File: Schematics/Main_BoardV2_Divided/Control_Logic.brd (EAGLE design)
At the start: 151.1 x 125.4 mm, 77 parts

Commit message: Visual Improvments
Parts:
- SV17: device con-lstb:MA08-1 -> pinhead:1X08
- SV23: device con-lstb:MA08-2 -> pinhead:2X08
- flipped JP12 to the top, turned to 180 degrees
- flipped JP13 to the top, turned to 180 degrees
- flipped JP5 to the top, turned to 180 degrees
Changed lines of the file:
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@@
 </layers>
 <board>
-<fusionsync huburn="a.cGVyc29uYWw6dWUyYzAxZDJj" projecturn="a.cGVyc29uYWw6dWUyYzAxZDJjIzIwMTkwNTA1MTkyMDg5NTI2" f3durn="urn:adsk.wipprod:dm.lineage:5vW4CCZ3SoaiVhg5slD4Gg" pcbguid="fc1e82cf-980c-4085-b012-4696e4d23687" lastpulledtime="" lastsyncedchangeguid="9388281c-1932-1015-b2ac-b4e115ec7e99"/>
+<fusionsync huburn="a.cGVyc29uYWw6dWUyYzAxZDJj" projecturn="a.cGVyc29uYWw6dWUyYzAxZDJjIzIwMTkwNTA1MTkyMDg5NTI2" f3durn="urn:adsk.wipprod:dm.lineage:5vW4CCZ3SoaiVhg5slD4Gg" pcbguid="fc1e82cf-980c-4085-b012-4696e4d23687" lastpulledtime="" lastsyncedchangeguid="d297562d-cfa8-3444-ce06-3ef9c99cdce7"/>
 <plain>
 <wire x1="0" y1="1.27" x2="151.11" y2="1.27" width="0" layer="20"/>
@@
 <attribute name="VALUE" x="44.45" y="105.41" size="0.9906" layer="27" ratio="10" rot="R90"/>
 </element>
-<element name="SV17" library="con-lstb" library_urn="urn:adsk.eagle:library:162" package="MA08-1" package3d_urn="urn:adsk.eagle:package:8343/1" value="" x="6.35" y="99.06" smashed="yes" rot="R90">
+<element name="SV17" library="pinhead" library_urn="urn:adsk.eagle:library:325" package="1X08" package3d_urn="urn:adsk.eagle:package:22409/2" value="" x="6.35" y="99.06" smashed="yes" rot="R90">
 <attribute name="MF" value="" x="6.35" y="99.06" size="1.778" layer="27" rot="R90" display="off"/>
 <attribute name="MPN" value="" x="6.35" y="99.06" size="1.778" layer="27" rot="R90" display="off"/>
@@
 <attribute name="VALUE" x="6.35" y="99.06" size="1.27" layer="27" ratio="10" rot="R90"/>
 </element>
-<element name="JP5" library="pinhead" library_urn="urn:adsk.eagle:library:325" package="1X02" package3d_urn="urn:adsk.eagle:package:22435/2" value="" x="113.03" y="115.57" smashed="yes" rot="MR0">
-<attribute name="NAME" x="115.6462" y="117.3988" size="1.27" layer="26" ratio="10" rot="MR0"/>
-<attribute name="VALUE" x="115.57" y="112.395" size="1.27" layer="28" rot="MR0"/>
+<element name="JP5" library="pinhead" library_urn="urn:adsk.eagle:library:325" package="1X02" package3d_urn="urn:adsk.eagle:package:22435/2" value="" x="113.03" y="115.57" smashed="yes" rot="R180">
+<attribute name="NAME" x="115.6462" y="113.7412" size="1.27" layer="25" ratio="10" rot="R180"/>
+<attribute name="VALUE" x="115.57" y="118.745" size="1.27" layer="27" rot="R180"/>
 </element>
 <element name="JP10" library="pinhead" library_urn="urn:adsk.eagle:library:325" package="1X02" package3d_urn="urn:adsk.eagle:package:22435/2" value="" x="6.35" y="71.12" smashed="yes" rot="R90">
@@
 <attribute name="VALUE" x="3.175" y="58.42" size="1.27" layer="27" rot="R270"/>
 </element>
-<element name="JP12" library="pinhead" library_urn="urn:adsk.eagle:library:325" package="1X02" package3d_urn="urn:adsk.eagle:package:22435/2" value="" x="120.65" y="115.57" smashed="yes" rot="MR0">
-<attribute name="NAME" x="123.2662" y="117.3988" size="1.27" layer="26" ratio="10" rot="MR0"/>
-<attribute name="VALUE" x="123.19" y="112.395" size="1.27" layer="28" rot="MR0"/>
-</element>
-<element name="JP13" library="pinhead" library_urn="urn:adsk.eagle:library:325" package="1X02" package3d_urn="urn:adsk.eagle:package:22435/2" value="" x="105.41" y="115.57" smashed="yes" rot="MR0">
-<attribute name="NAME" x="108.0262" y="117.3988" size="1.27" layer="26" ratio="10" rot="MR0"/>
-<attribute name="VALUE" x="107.95" y="112.395" size="1.27" layer="28" rot="MR0"/>
+<element name="JP12" library="pinhead" library_urn="urn:adsk.eagle:library:325" package="1X02" package3d_urn="urn:adsk.eagle:package:22435/2" value="" x="120.65" y="115.57" smashed="yes" rot="R180">
+<attribute name="NAME" x="123.2662" y="113.7412" size="1.27" layer="25" ratio="10" rot="R180"/>
+<attribute name="VALUE" x="123.19" y="118.745" size="1.27" layer="27" rot="R180"/>
+</element>
+<element name="JP13" library="pinhead" library_urn="urn:adsk.eagle:library:325" package="1X02" package3d_urn="urn:adsk.eagle:package:22435/2" value="" x="105.41" y="115.57" smashed="yes" rot="R180">
+<attribute name="NAME" x="108.0262" y="113.7412" size="1.27" layer="25" ratio="10" rot="R180"/>
+<attribute name="VALUE" x="107.95" y="118.745" size="1.27" layer="27" rot="R180"/>
 </element>
 <element name="JP14" library="pinhead" library_urn="urn:adsk.eagle:library:325" package="1X02" package3d_urn="urn:adsk.eagle:package:22435/2" value="" x="6.35" y="63.5" smashed="yes" rot="R90">
@@
 <attribute name="VALUE" x="9.525" y="60.96" size="1.27" layer="27" rot="R90"/>
 </element>
-<element name="SV23" library="con-lstb" library_urn="urn:adsk.eagle:library:162" package="MA08-2" package3d_urn="urn:adsk.eagle:package:8335/1" value="" x="142.24" y="39.37" smashed="yes" rot="R270">
+<element name="SV23" library="pinhead" library_urn="urn:adsk.eagle:library:325" package="2X08" package3d_urn="urn:adsk.eagle:package:22481/2" value="" x="142.24" y="39.37" smashed="yes" rot="R270">
 <attribute name="MF" value="" x="142.24" y="39.37" size="1.778" layer="27" rot="R270" display="off"/>
 <attribute name="MPN" value="" x="142.24" y="39.37" size="1.778" layer="27" rot="R270" display="off"/>
@@
 <wire x1="95.5548" y1="98.933" x2="111.2393" y2="114.6175" width="0.254" layer="1"/>
 <wire x1="92.9005" y1="90.2462" x2="92.9005" y2="96.2787" width="0.254" layer="1"/>
-<wire x1="111.7219" y1="115.3414" x2="111.76" y2="115.57" width="0.254" layer="1"/>
+<wire x1="111.7219" y1="115.3414" x2="111.76" y2="115.57" width="0.254" layer="16"/>
 <wire x1="92.9005" y1="90.2462" x2="92.71" y2="90.17" width="0.254" layer="1"/>
 <wire x1="125.7173" y1="71.9074" x2="125.7173" y2="71.1835" width="0.254" layer="1"/>
@@
 <wire x1="128.511984375" y1="18.427015625" x2="128.27" y2="18.427015625" width="0.254" layer="16"/>
 <wire x1="128.141284375" y1="18.869796875" x2="128.27" y2="18.427015625" width="0.254" layer="16"/>
+<wire x1="111.7219" y1="115.3414" x2="111.7219" y2="115.3414" width="0" layer="19" extent="1-16"/>
 </signal>
 <signal name="INST_REGISTER1:VCC">
@@
 <wire x1="74.5617" y1="50.9143" x2="89.7636" y2="66.1162" width="0.254" layer="1"/>
 <wire x1="73.8378" y1="50.9143" x2="74.5617" y2="50.9143" width="0.254" layer="1"/>
-<wire x1="104.0003" y1="115.3414" x2="104.14" y2="115.57" width="0.254" layer="16"/>
+<wire x1="104.0003" y1="115.3414" x2="104.14" y2="115.57" width="0.254" layer="1"/>
 <wire x1="73.8378" y1="50.9143" x2="73.66" y2="50.8" width="0.254" layer="1"/>
 <via x="89.7636" y="66.1162" extent="1-16" drill="0.35"/>
@@
 <contactref element="CONTROL_LOGIC1:IC5" pad="9"/>
 <contactref element="CONTROL_LOGIC1:IC5" pad="10"/>
+<wire x1="104.0003" y1="115.3414" x2="104.0003" y2="115.3414" width="0" layer="19" extent="1-16"/>
 </signal>
 <signal name="PC_LE">
@@
 <wire x1="32.0929" y1="110.7567" x2="55.7403" y2="110.7567" width="0.254" layer="16"/>
 <wire x1="30.1625" y1="108.8263" x2="32.0929" y2="110.7567" width="0.254" layer="16"/>
-<wire x1="106.6546" y1="115.5827" x2="106.68" y2="115.57" width="0.254" layer="16"/>
+<wire x1="106.6546" y1="115.5827" x2="106.68" y2="115.57" width="0.254" layer="1"/>
 <via x="37.6428" y="76.4921" extent="1-16" drill="0.35"/>
 <contactref element="INST_REGISTER1:IC2" pad="15"/>
 <contactref element="INST_REGISTER1:IC3" pad="15"/>
 <contactref element="CONTROL_LOGIC1:IC5" pad="8"/>
+<wire x1="106.6546" y1="115.5827" x2="106.6546" y2="115.5827" width="0" layer="19" extent="1-16"/>
 </signal>
 <signal name="|AWRITE">
@@
 <wire x1="129.8194" y1="59.1185" x2="129.8194" y2="106.4133" width="0.254" layer="1"/>
 <wire x1="128.8542" y1="58.1533" x2="129.8194" y2="59.1185" width="0.254" layer="1"/>
-<wire x1="122.0978" y1="115.3414" x2="121.92" y2="115.57" width="0.254" layer="1"/>
+<wire x1="122.0978" y1="115.3414" x2="121.92" y2="115.57" width="0.254" layer="16"/>
 <via x="128.8542" y="58.1533" extent="1-16" drill="0.35"/>
 <contactref element="CONTROL_LOGIC1:IC2" pad="8"/>
 <contactref element="CONTROL_LOGIC1:IC1" pad="8"/>
+<wire x1="122.0978" y1="115.3414" x2="122.0978" y2="115.3414" width="0" layer="19" extent="1-16"/>
 </signal>
 <signal name="CF">
@@
 <wire x1="128.8542" y1="68.0466" x2="128.8542" y2="105.6894" width="0.254" layer="1"/>
 <wire x1="128.1303" y1="67.3227" x2="128.8542" y2="68.0466" width="0.254" layer="16"/>
-<wire x1="119.4435" y1="115.3414" x2="119.38" y2="115.57" width="0.254" layer="1"/>
+<wire x1="119.4435" y1="115.3414" x2="119.38" y2="115.57" width="0.254" layer="16"/>
 <via x="127.1651" y="39.5732" extent="1-16" drill="0.35"/>
 <via x="128.8542" y="68.0466" extent="1-16" drill="0.35"/>
 <contactref element="CONTROL_LOGIC1:IC2" pad="7"/>
 <contactref element="CONTROL_LOGIC1:IC1" pad="7"/>
+<wire x1="119.4435" y1="115.3414" x2="119.4435" y2="115.3414" width="0" layer="19" extent="1-16"/>
 </signal>
 <signal name="RAM_LRS">

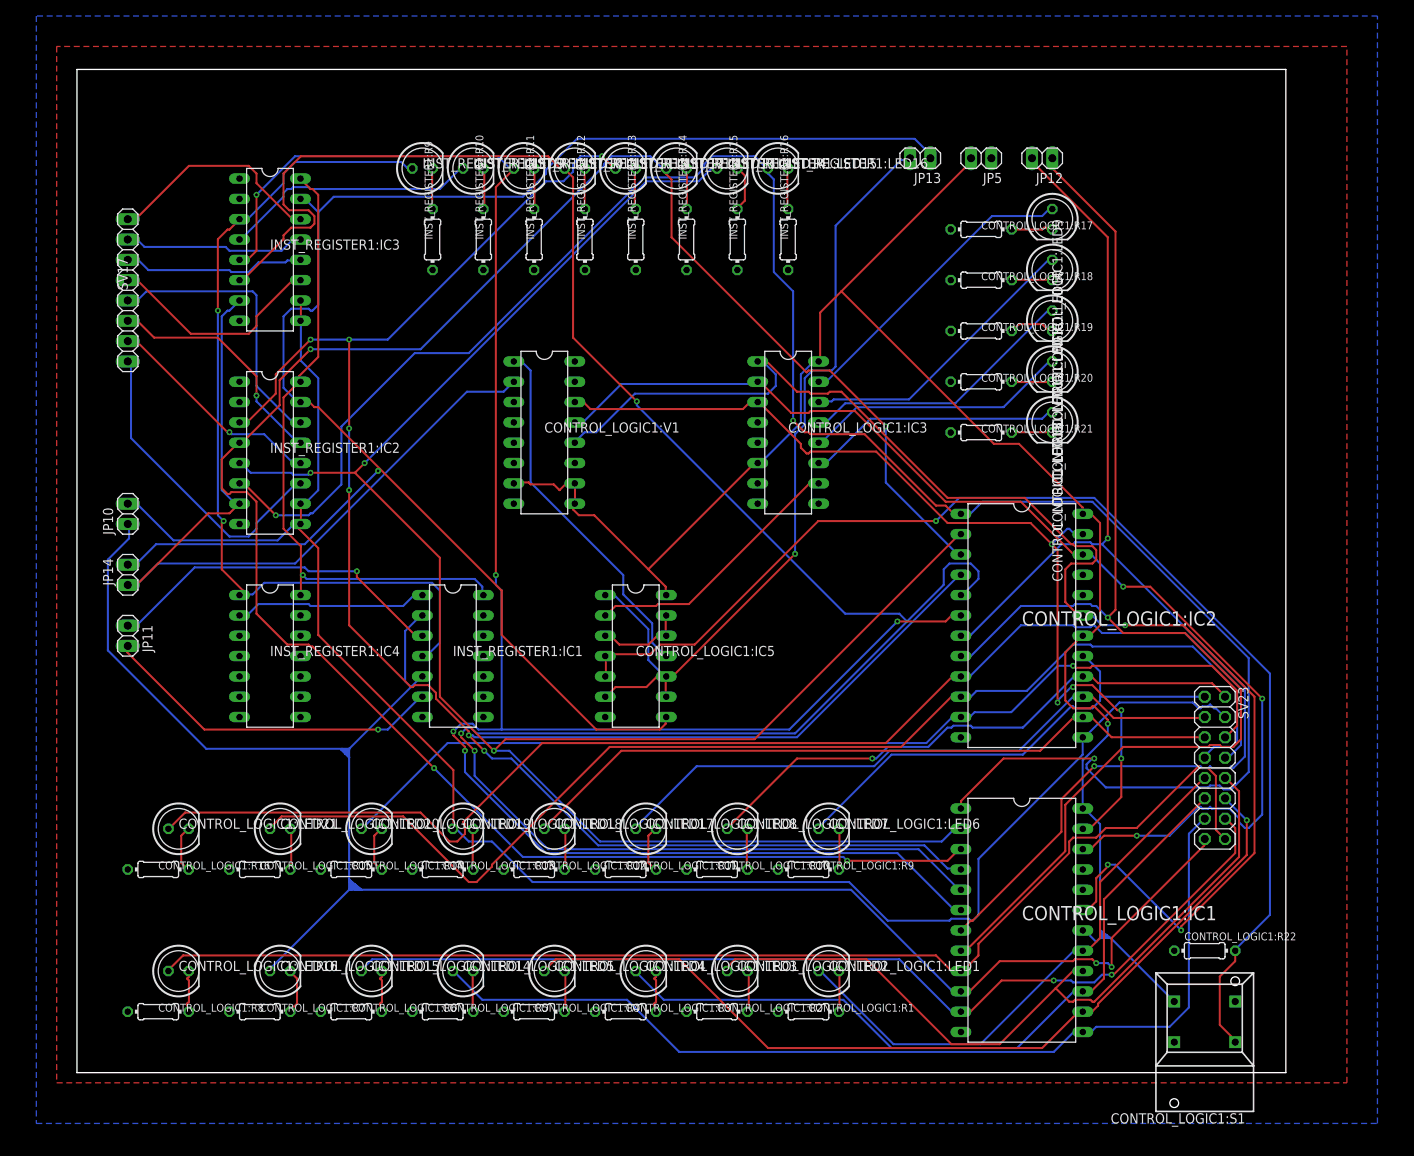
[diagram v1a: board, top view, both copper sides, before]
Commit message: Microcode Added and Ram Updated
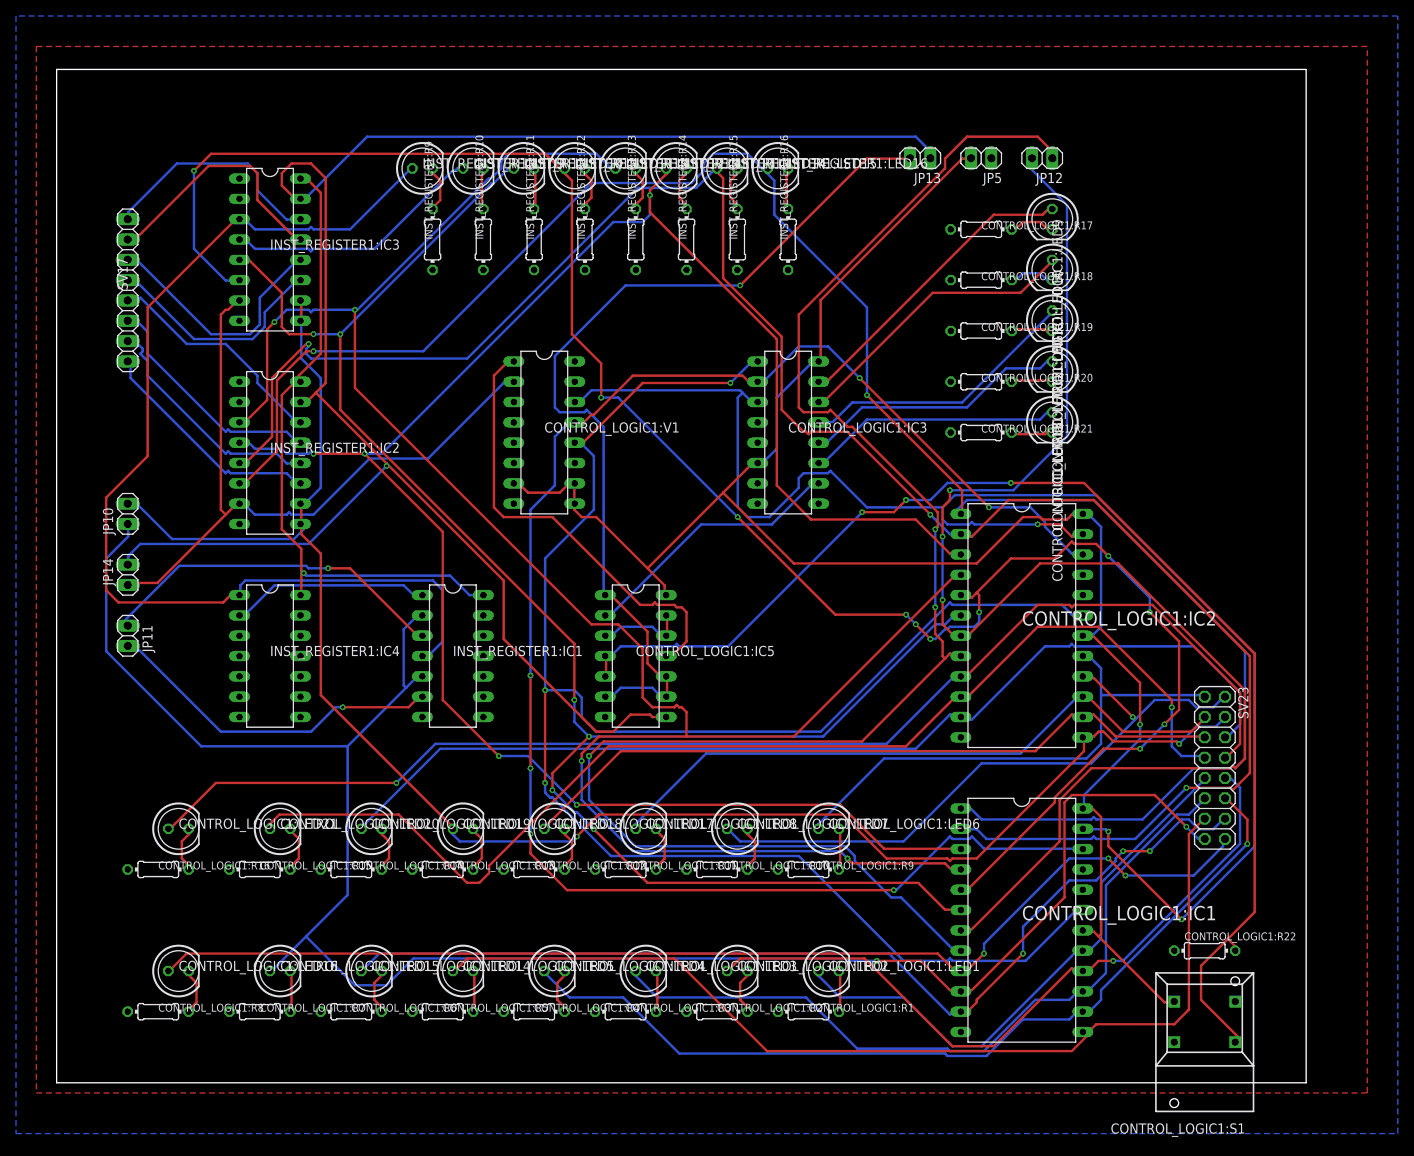
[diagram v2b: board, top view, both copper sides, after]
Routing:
- net CONTROL_LOGIC1:N$3: track 121.0 -> 193.1 mm, vias 5 -> 3
- net CONTROL_LOGIC1:N$2: track 146.1 -> 210.5 mm, vias 3 -> 6
- net CONTROL_LOGIC1:N$1: track 176.0 -> 231.8 mm
- net ZF: track 159.1 -> 208.9 mm, vias 1 -> 3
- net N$33: track 289.3 -> 242.1 mm, vias 3 -> 11
- net N$32: track 260.6 -> 231.0 mm, vias 5 -> 6
- net INST_REGISTER1:SLC_REG: track 111.1 -> 134.1 mm, vias 2 -> 0
- net CF: track 156.5 -> 176.1 mm, vias 2 -> 3
- net N$35: track 264.1 -> 248.0 mm, vias 4 -> 5
- net CLK: track 104.6 -> 88.7 mm
- net CLR: track 216.9 -> 229.7 mm
- net N$37: track 253.1 -> 241.5 mm, vias 3 -> 2
- net CONTROL_LOGIC1:N$8: track 45.4 -> 56.5 mm
- net HLT: track 154.1 -> 143.7 mm, vias 0 -> 3
- net 8B_8: track 39.2 -> 29.1 mm
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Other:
- board size 151.1 x 125.4 mm -> 156.2 x 126.7 mm
